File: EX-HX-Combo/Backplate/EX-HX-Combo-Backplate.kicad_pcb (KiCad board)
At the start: 2 copper layers, 17.5 x 124.5 mm, 1 part

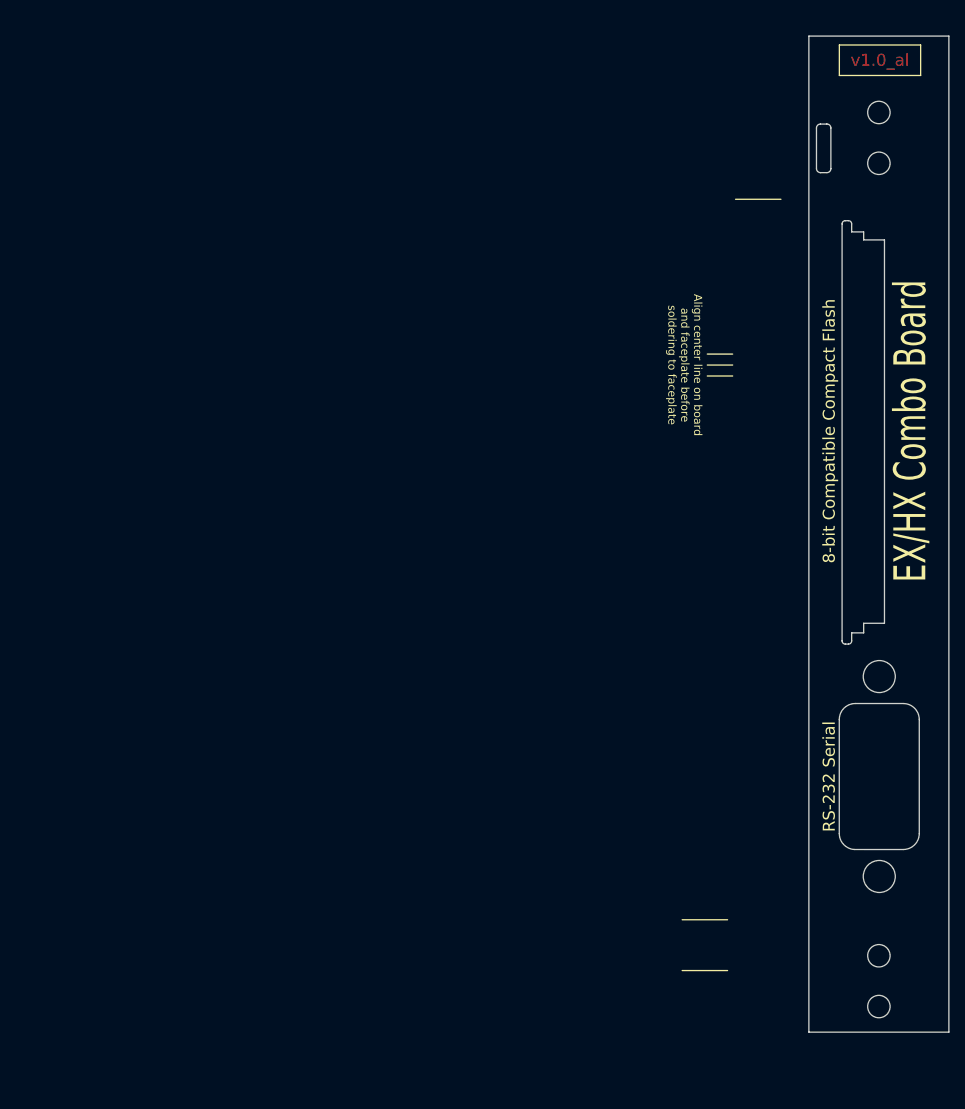
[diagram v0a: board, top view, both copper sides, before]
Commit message: Work on EX-HX-Combo backplate. Made a panel, however JLCPCB can't determine the board outline and do not know how to specify the v-score across the top and bottom.
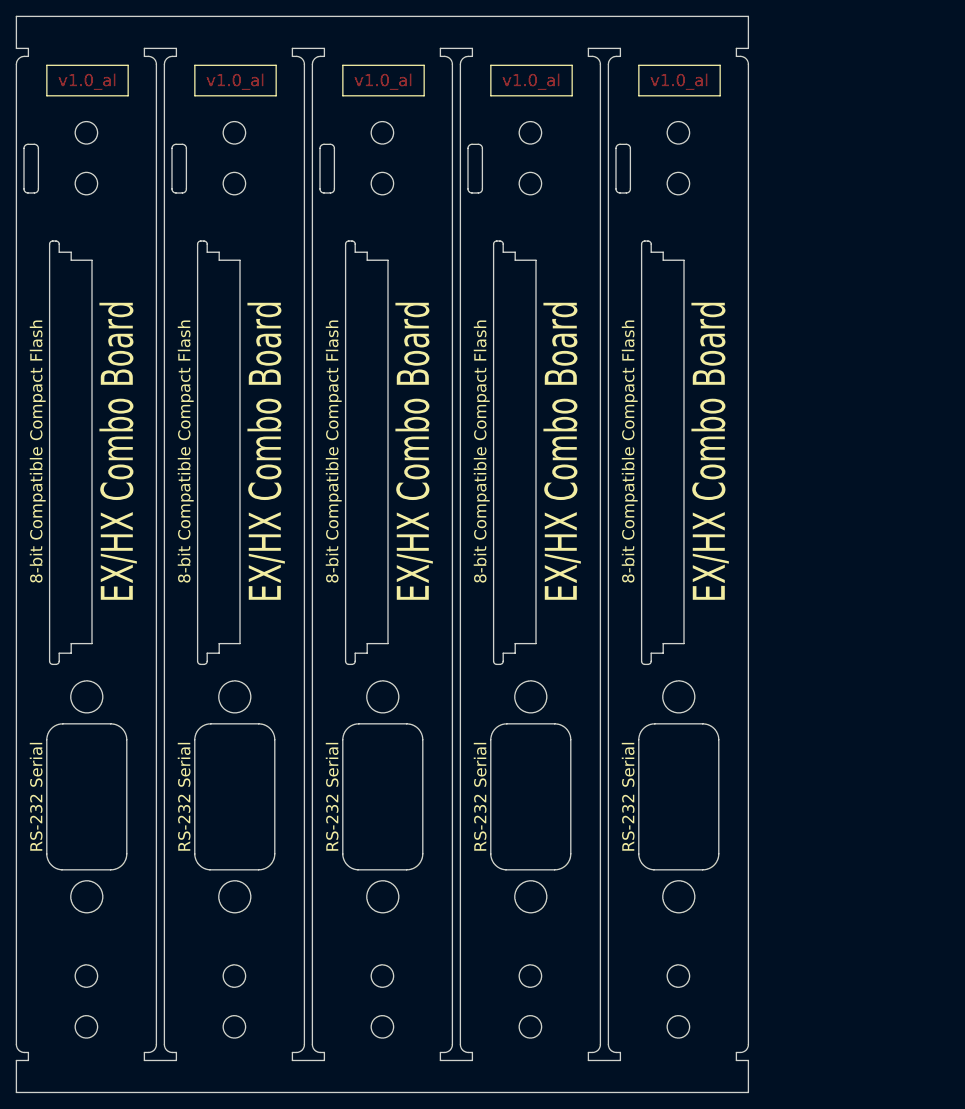
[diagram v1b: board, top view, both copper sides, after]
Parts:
- removed H8: DB-9 Faceplate, 00Custom:DB9_Face_NPTH
- added H1: Serial Port Holes, 00Custom:DB9_Face_NPTH, F.Cu at (230.2, 122.6)
- added H1: Serial Port Holes, 00Custom:DB9_Face_NPTH, F.Cu at (211.7, 122.6)
- added H1: Serial Port Holes, 00Custom:DB9_Face_NPTH, F.Cu at (193.2, 122.6)
- added H1: Serial Port Holes, 00Custom:DB9_Face_NPTH, F.Cu at (174.7, 122.6)
- added H1: Serial Port Holes, 00Custom:DB9_Face_NPTH, F.Cu at (156.2, 122.6)
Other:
- board size 17.5 x 124.5 mm -> 91.5 x 134.5 mm
- board text removed: "Maxium recommended length. This will almost reach the ROM when a SmartWatch is fitted in an HX. Tall components this far back will hit the top of the case when the board is in the top position."

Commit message: EX-HX-Combo: Single backplate for testing.
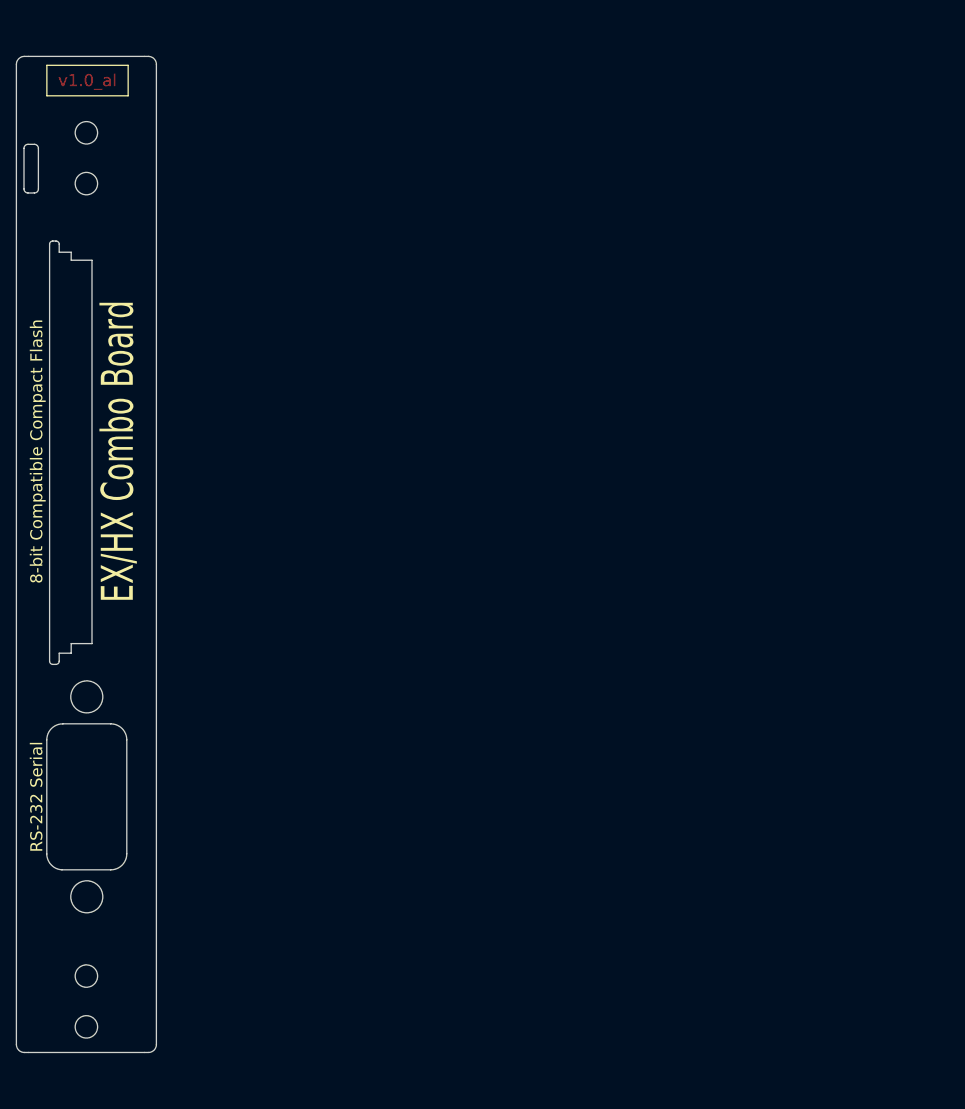
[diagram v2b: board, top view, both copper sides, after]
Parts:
- removed the H1 at (230.2, 122.6)
- removed the H1 at (211.7, 122.6)
- removed the H1 at (193.2, 122.6)
- removed the H1 at (174.7, 122.6)
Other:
- board size 91.5 x 134.5 mm -> 17.5 x 124.5 mm
